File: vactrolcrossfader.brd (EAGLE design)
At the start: 27.9 x 80.5 mm, 56 parts, among them U1 TL072_SMD

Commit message: board done
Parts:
- JP2: value M05X2PTH -> EURO_POWER_HEADERFAT_PADS; device og-header:AVR_ICSP -> MusicThingModular:EURO_PWR_HEADER_FAT
- moved JP2 0.40 mm to (13.8, 73.0), flipped to the bottom, turned to 270 degrees
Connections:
- net N$56: now also D8.C; no longer D7.A
- net N$64: now also D7.A; no longer D8.C
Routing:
- net N$41: track 33.7 -> 81.7 mm
- net N$32: track 39.5 -> 72.8 mm
- net N$13: track 42.7 -> 64.1 mm, vias 2 -> 0
- net VCC: track 136.3 -> 117.8 mm, vias 4 -> 3
- net N$30: track 31.0 -> 12.9 mm
- net N$11: track 81.9 -> 64.8 mm
- net N$36: track 33.3 -> 50.1 mm, vias 3 -> 1
- net N$12: track 68.7 -> 53.3 mm
- net N$25: track 46.5 -> 31.2 mm, vias 0 -> 3
- net N$27: track 29.4 -> 43.8 mm, vias 2 -> 0
- net GND: track 254.5 -> 242.5 mm, vias 2 -> 0
- net N$3: track 43.4 -> 49.1 mm, vias 3 -> 2
- net N$8: track 21.6 -> 17.3 mm, vias 2 -> 0
- net N$9: track 17.1 -> 12.9 mm, vias 1 -> 0
- net N$4: track 8.89 -> 5.14 mm
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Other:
- board text added: "DOUBLE CROSSED !!!"
- board text added: "Designed in København, Denmark 2016."
- board text added: "Guess what! I got a fever! And the only prescription is more vactrols!"
- board text added: "Inspired by: Don Buchla& Mark Verbos& Olivier Gillet& Tom Whitwell& Pusherman"
- board text added: "Vactrol crossfader by Mads Kjeldgaard. V1."
- board text removed: "DOUBLE CROSSED Vactrol x-fader, v1 By Mads Kjeldgaard"
- board text removed: "Designed in København, Denmark. Thx Don Buchla, Mark Verbos, Olivier Gillet"

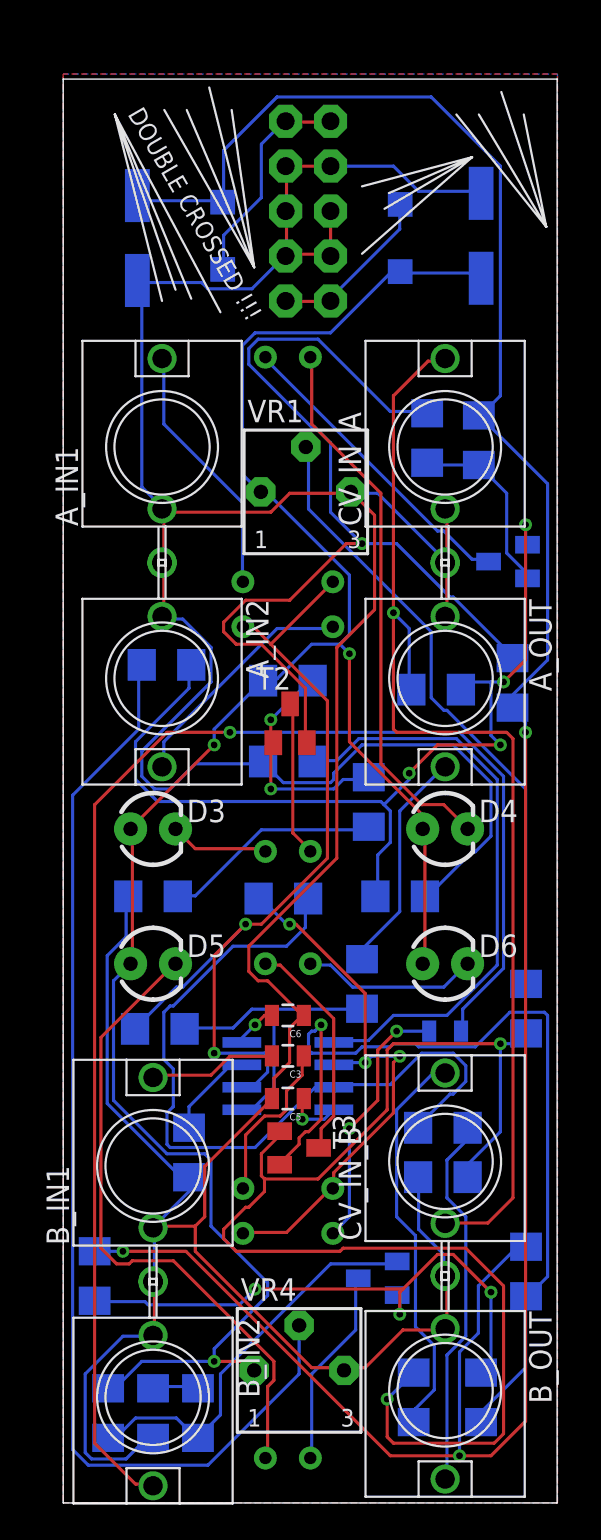
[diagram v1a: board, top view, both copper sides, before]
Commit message: updated board to v 1.1: Better silk screen legibility on smd components, trimmers moved to backside
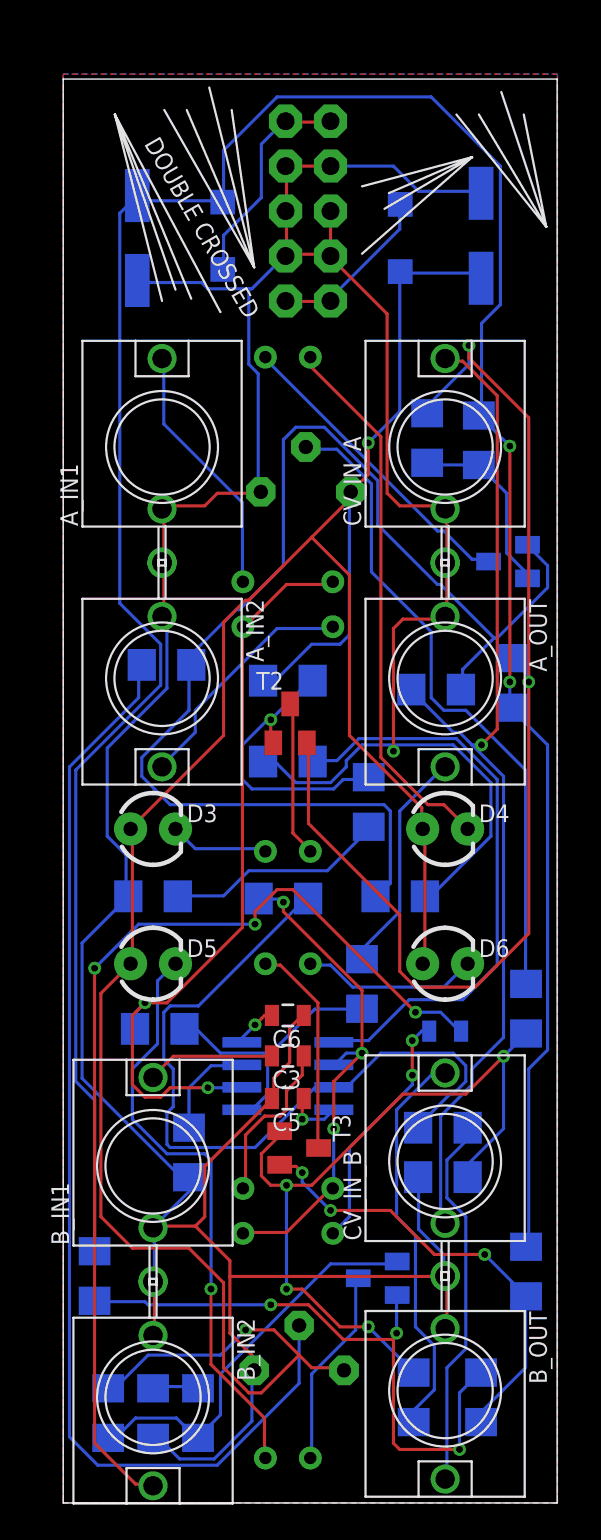
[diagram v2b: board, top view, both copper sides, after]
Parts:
- flipped VR1 to the bottom
- flipped VR4 to the bottom
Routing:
- net N$32: track 72.8 -> 44.4 mm, vias 2 -> 4
- net N$36: track 50.1 -> 25.5 mm, vias 1 -> 3
- net N$41: track 81.7 -> 57.4 mm, vias 1 -> 3
- net VCC: track 117.8 -> 140.9 mm, vias 3 -> 2
- net GND: track 242.5 -> 220.4 mm, vias 0 -> 1
- net N$12: track 53.3 -> 71.9 mm, vias 4 -> 0
- net VEE: track 144.3 -> 153.7 mm, vias 3 -> 2
- net N$16: track 56.3 -> 65.2 mm, vias 1 -> 2
- net N$11: track 64.8 -> 58.6 mm
- net N$3: track 49.1 -> 43.7 mm
- net N$15: track 13.3 -> 16.6 mm, vias 2 -> 1
- net N$25: track 31.2 -> 28.2 mm
- net N$35: track 32.1 -> 35.1 mm
- net N$29: track 36.1 -> 33.3 mm, vias 0 -> 1
- net N$33: track 35.6 -> 37.2 mm
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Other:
- board text added: "DOUBLE CROSSED"
- board text added: "Vactrol crossfader by Mads Kjeldgaard. V1.1"
- board text removed: "DOUBLE CROSSED !!!"
- board text removed: "Vactrol crossfader by Mads Kjeldgaard. V1."

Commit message: Prototype board updated and sent to fab
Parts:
- moved VR4 69.8 mm to (23.2, 76.6)
- moved VR1 21.6 mm to (3.56, 76.2)
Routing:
- net VEE: track 153.7 -> 100.4 mm, vias 2 -> 6
- net N$16: track 65.2 -> 34.2 mm
- net N$33: track 37.2 -> 60.3 mm, vias 0 -> 1
- net N$12: track 71.9 -> 49.4 mm
- net N$13: track 64.2 -> 41.9 mm
- net VCC: track 140.9 -> 150.5 mm, vias 2 -> 1
- net GND: track 220.4 -> 229.1 mm
- net N$41: track 57.4 -> 49.3 mm, vias 3 -> 2
- net N$29: track 33.3 -> 39.6 mm, vias 1 -> 0
- net N$32: track 44.4 -> 48.0 mm
- net N$3: track 43.7 -> 46.3 mm
- net N$46: track 13.9 -> 15.4 mm, vias 2 -> 3
- net N$36: track 25.5 -> 27.0 mm
- net N$30: track 12.1 -> 13.5 mm
- net N$10: track 17.5 -> 18.9 mm
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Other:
- board text added: "BALANCE TRIM_A"
- board text added: "BALANCE TRIM_B"

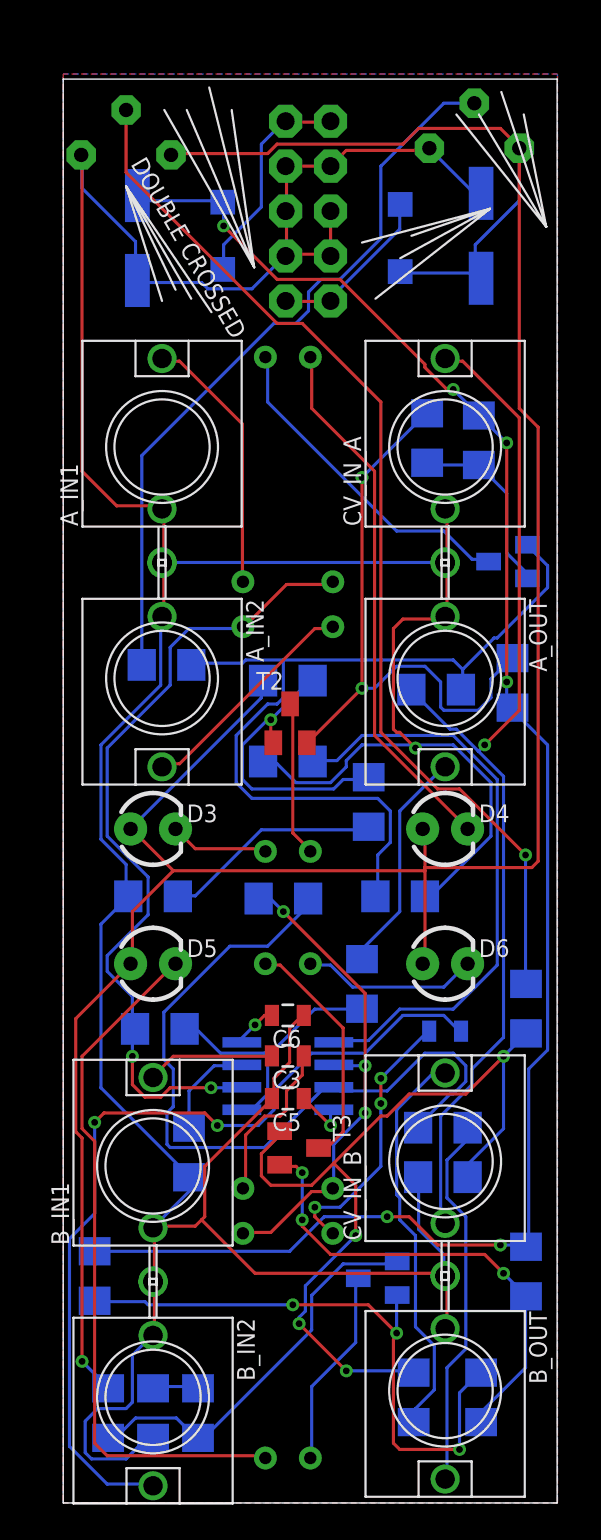
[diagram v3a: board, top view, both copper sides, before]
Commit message: Moved power caps to make room for trimmers
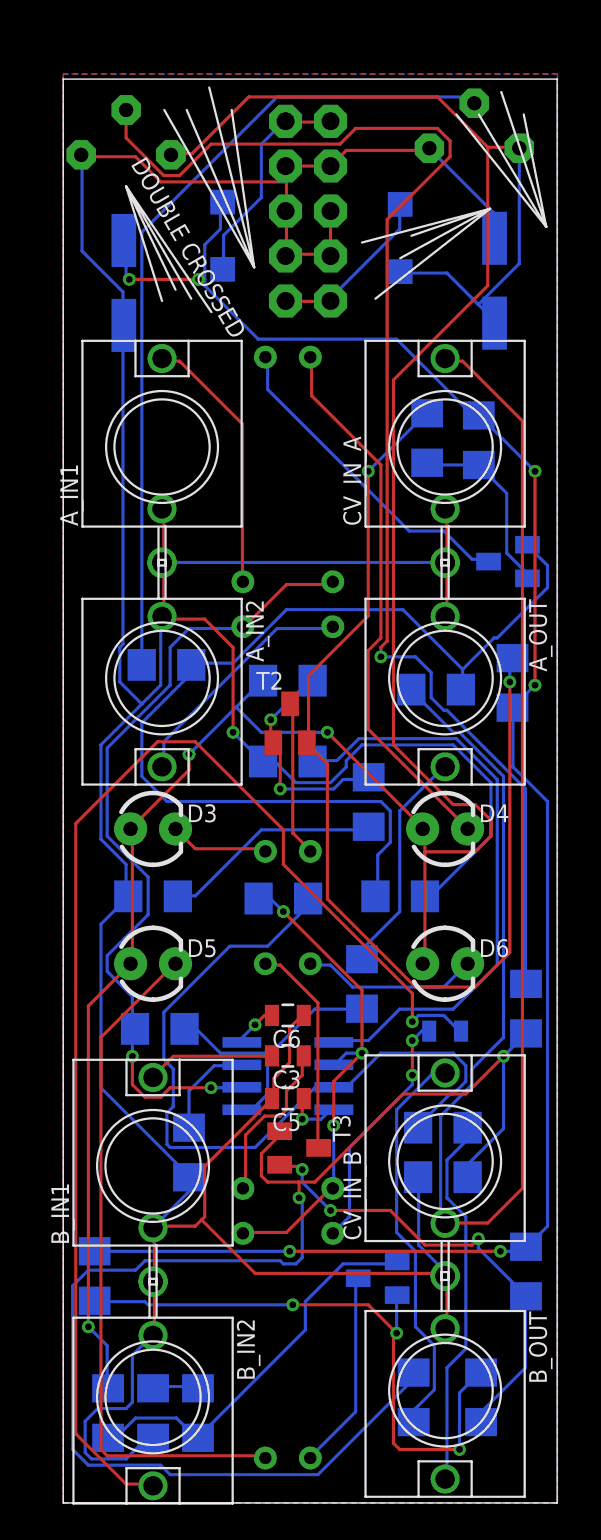
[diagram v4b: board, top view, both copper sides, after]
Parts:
- moved C25 2.65 mm to (24.4, 69.1)
- moved C30 2.65 mm to (3.43, 69.0)
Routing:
- net N$32: track 48.0 -> 79.1 mm, vias 4 -> 2
- net N$11: track 59.5 -> 88.5 mm, vias 1 -> 0
- net N$16: track 34.2 -> 60.7 mm
- net N$41: track 49.3 -> 72.9 mm, vias 2 -> 1
- net N$33: track 60.3 -> 76.1 mm
- net GND: track 229.1 -> 237.4 mm
- net N$12: track 49.4 -> 56.4 mm
- net N$13: track 41.9 -> 46.6 mm
- net VEE: track 100.4 -> 105.0 mm
- net N$15: track 16.6 -> 12.9 mm, vias 1 -> 2
- net VCC: track 150.5 -> 152.8 mm, vias 1 -> 3
- net N$46: track 15.4 -> 13.9 mm, vias 3 -> 2
- net N$30: track 13.5 -> 12.1 mm
- net N$29: track 39.6 -> 38.8 mm
- net N$36: track 27.0 -> 26.2 mm
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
